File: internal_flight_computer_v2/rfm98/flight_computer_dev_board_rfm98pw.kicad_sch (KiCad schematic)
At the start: 95 parts, among them IC1 RP2040_QFN56, IC2 AZ1117CH-3.3TRG1, J1 Conn_ARM_JTAG_SWD_10, J10 BM04B-SRSS-TB(LF)(SN), J11 BM04B-SRSS-TB(LF)(SN), J12 BM04B-SRSS-TB(LF)(SN), J13 Breakout, J15 Battery, J2 FC to EPS Connector, J3 Life Makes Lemonade, J4 104031-0811, J5 BM04B-SRSS-TB(LF)(SN), J6 Conn_Coaxial, J7 Breakout, J8 USB_B_Micro, J9 BM04B-SRSS-TB(LF)(SN), SW1 KMR2, SW2 KMR2, U10 AP3602AKTR-G1, U3 MAX706RESA, U4 RFM98PW, U5 RFM9xBreakout, U6 W25Q128JV, U7 LSM6DSOTR, U8 LSM303AGRTR, U9 MCP25625-E/ML, Y1 12MHZ, Y3 16MHZ 12 pf

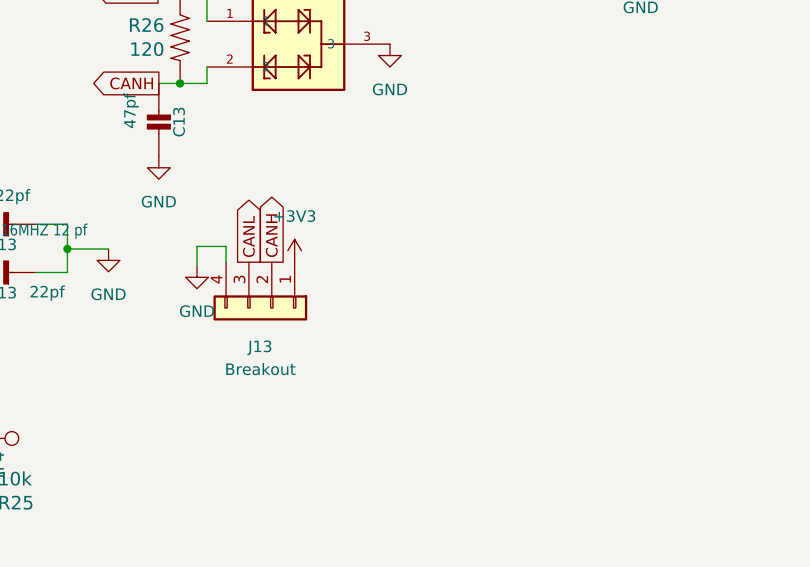
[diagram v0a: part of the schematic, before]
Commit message: Huge Restructure of Dev Boards
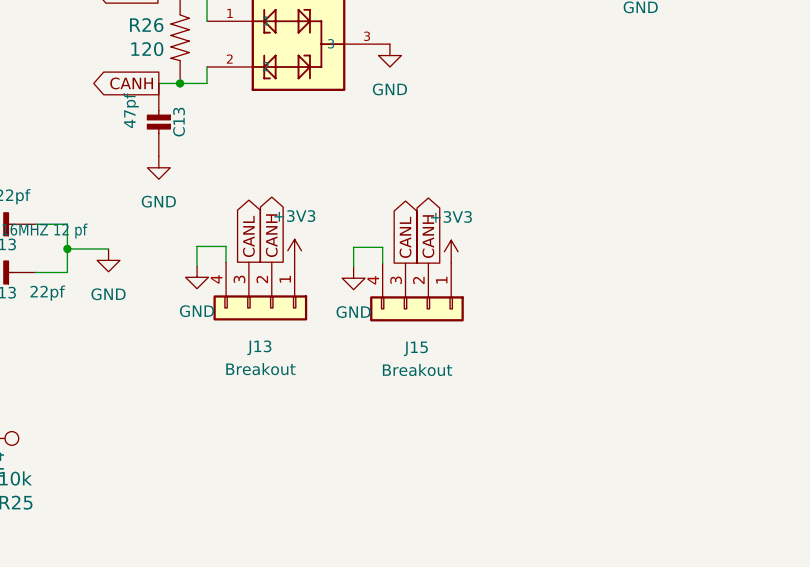
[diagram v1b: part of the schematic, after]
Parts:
- added J15: Breakout, Connector_JST:JST_SH_BM04B-SRSS-TB_1x04-1MP_P1.00mm_Vertical, symbol Connector_Generic:Conn_01x04
- J13: footprint Connector_JST:JST_SH_SM04B-SRSS-TB_1x04-1MP_P1.00mm_Horizontal -> Connector_JST:JST_SH_BM04B-SRSS-TB_1x04-1MP_P1.00mm_Vertical
- TP5: value RESET -> 5V
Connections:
- net +3V3: now also J15.1 (Pin_1)
- net CANH: now also J15.2 (Pin_2)
- net CANL: now also J15.3 (Pin_3)
- net GND: now also J15.4 (Pin_4)
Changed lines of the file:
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@@
     (stroke (width 0) (type default))
   )
+  (wire (pts (xy 406.8318 351.409) (xy 406.8318 353.1616))
+    (stroke (width 0) (type default))
+  )
   (wire (pts (xy 359.3592 348.9706) (xy 352.2218 348.9706))
     (stroke (width 0) (type default))
@@
     (stroke (width 0) (type default))
   )
+  (wire (pts (xy 403.606 351.409) (xy 406.8318 351.409))
+    (stroke (width 0) (type default))
+  )
   (wire (pts (xy 385.572 234.569) (xy 394.3604 234.569))
     (stroke (width 0) (type default))
@@
     (stroke (width 0) (type default))
   )
+  (wire (pts (xy 403.606 351.409) (xy 403.606 353.568))
+    (stroke (width 0) (type default))
+  )
   (wire (pts (xy 142.748 250.444) (xy 142.748 247.904))
     (stroke (width 0) (type default))
@@
     )
   )
+  (global_label "CANH" (shape output) (at 411.9118 353.1616 90) (fields_autoplaced)
+    (effects (font (size 1.27 1.27)) (justify left))
+    (property "Intersheetrefs" "${INTERSHEET_REFS}" (at 411.9118 345.2362 90)
+      (effects (font (size 1.27 1.27)) (justify left) hide)
+    )
+  )
   (global_label "CANL" (shape output) (at 391.9728 353.06 90) (fields_autoplaced)
     (effects (font (size 1.27 1.27)) (justify left))
@@
     )
   )
+  (global_label "CANL" (shape output) (at 409.3718 353.1616 90) (fields_autoplaced)
+    (effects (font (size 1.27 1.27)) (justify left))
+    (property "Intersheetrefs" "${INTERSHEET_REFS}" (at 409.3718 345.5386 90)
+      (effects (font (size 1.27 1.27)) (justify left) hide)
+    )
+  )
   (global_label "SDA0" (shape bidirectional) (at 153.924 131.826 0) (fields_autoplaced)
     (effects (font (size 1.27 1.27)) (justify left))
@@
     )
   )
+  (symbol (lib_id "power:GND") (at 403.606 353.568 0) (unit 1)
+    (in_bom yes) (on_board yes) (dnp no) (fields_autoplaced)
+    (property "Reference" "#PWR036" (at 403.606 359.918 0)
+      (effects (font (size 1.27 1.27)) hide)
+    )
+    (property "Value" "GND" (at 403.606 358.648 0)
+      (effects (font (size 1.27 1.27)))
+    )
+    (property "Footprint" "" (at 403.606 353.568 0)
+      (effects (font (size 1.27 1.27)) hide)
+    )
+    (property "Datasheet" "" (at 403.606 353.568 0)
+      (effects (font (size 1.27 1.27)) hide)
+    )
+    (pin "1")
+    (instances
+      (project "flight_computer_dev_board_rfm98pw"
+        (path "/c64c0d72-a9f6-4f3a-891e-1f647558f538"
+          (reference "#PWR036") (unit 1)
+        )
+      )
+    )
+  )
   (symbol (lib_id "Adafruit ItsyBitsy RP2040-eagle-import:+3V3") (at 153.543 34.925 0) (unit 1)
     (in_bom yes) (on_board yes) (dnp no) (fields_autoplaced)
@@
     )
   )
+  (symbol (lib_id "Connector_Generic:Conn_01x04") (at 411.9118 358.2416 270) (unit 1)
+    (in_bom yes) (on_board yes) (dnp no) (fields_autoplaced)
+    (property "Reference" "J15" (at 410.6418 362.5596 90)
+      (effects (font (size 1.27 1.27)))
+    )
+    (property "Value" "Breakout" (at 410.6418 365.0996 90)
+      (effects (font (size 1.27 1.27)))
+    )
+    (property "Footprint" "Connector_JST:JST_SH_BM04B-SRSS-TB_1x04-1MP_P1.00mm_Vertical" (at 411.9118 358.2416 0)
+      (effects (font (size 1.27 1.27)) hide)
+    )
+    (property "Datasheet" "~" (at 411.9118 358.2416 0)
+      (effects (font (size 1.27 1.27)) hide)
+    )
+    (pin "1")
+    (pin "2")
+    (pin "3")
+    (pin "4")
+    (instances
+      (project "flight_computer_dev_board_rfm98pw"
+        (path "/c64c0d72-a9f6-4f3a-891e-1f647558f538"
+          (reference "J15") (unit 1)
+        )
+      )
+    )
+  )
   (symbol (lib_id "Connector:TestPoint") (at 22.987 97.536 270) (unit 1)
     (in_bom yes) (on_board yes) (dnp no)
@@
       (effects (font (size 1.27 1.27)) (justify left))
     )
-    (property "Value" "RESET" (at 236.982 347.7768 0)
+    (property "Value" "5V" (at 236.982 347.7768 0)
       (effects (font (size 1.27 1.27)) (justify left) hide)
     )
@@
     )
   )
+  (symbol (lib_id "power:+3V3") (at 414.4518 353.1616 0) (unit 1)
+    (in_bom yes) (on_board yes) (dnp no) (fields_autoplaced)
+    (property "Reference" "#PWR037" (at 414.4518 356.9716 0)
+      (effects (font (size 1.27 1.27)) hide)
+    )
+    (property "Value" "+3V3" (at 414.4518 348.0816 0)
+      (effects (font (size 1.27 1.27)))
+    )
+    (property "Footprint" "" (at 414.4518 353.1616 0)
+      (effects (font (size 1.27 1.27)) hide)
+    )
+    (property "Datasheet" "" (at 414.4518 353.1616 0)
+      (effects (font (size 1.27 1.27)) hide)
+    )
+    (pin "1")
+    (instances
+      (project "flight_computer_dev_board_rfm98pw"
+        (path "/c64c0d72-a9f6-4f3a-891e-1f647558f538"
+          (reference "#PWR037") (unit 1)
+        )
+      )
+    )
+  )
   (symbol (lib_id "BM04B-SRSS-TB_LF__SN_:BM04B-SRSS-TB(LF)(SN)") (at 221.615 74.676 0) (unit 1)
     (in_bom yes) (on_board yes) (dnp no) (fields_autoplaced)
@@
       (effects (font (size 1.27 1.27)))
     )
-    (property "Footprint" "Connector_JST:JST_SH_SM04B-SRSS-TB_1x04-1MP_P1.00mm_Horizontal" (at 394.5128 358.14 0)
+    (property "Footprint" "Connector_JST:JST_SH_BM04B-SRSS-TB_1x04-1MP_P1.00mm_Vertical" (at 394.5128 358.14 0)
       (effects (font (size 1.27 1.27)) hide)
     )

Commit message: Big Update of In Dev Boards
Mid Term update for all the boards being developed for use by the Irvington Team on Pleiades - Orpheus
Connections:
- net USBBOOT is gone; now on net D3: D4.1 (K), IC1.16 (GPIO13), SW1.A (P), SW1.A' (P1), TP1.1
- net 3v3 Spec: no longer LED1.1 (VDD)
- net D6: now also IC1.27 (GPIO16); no longer IC1.29 (GPIO18)
- net D8: now also IC1.29 (GPIO18); no longer IC1.30 (GPIO19)
- net D9: now also IC1.30 (GPIO19); no longer IC1.39 (GPIO27/AD1)
- net BURN_RELAY_A / VS renamed BURN_RELAY_A / D5
- net BURN_RELAY_A / D5: now also JP9.3 (B); no longer J2.2 (Pin_2)
- net D4 renamed VBUS_RESET / D4
- net VBUS_RESET / D4: now also IC1.17 (GPIO14); no longer IC1.27 (GPIO16)
- net D5 renamed D7
- net D7: now also J2.9 (Pin_9); no longer JP9.3 (B)
- net ENABLE_BURN / D7 renamed ENABLE_BURN / PC
- net ENABLE_BURN / PC: now also J2.3 (Pin_3); no longer J2.9 (Pin_9)
- net ENAB_RF / D3 renamed D3
- net D3: no longer IC1.15 (GPIO12)
- net I2C_RESET / D2 renamed ENAB_RF / D2
- net ENAB_RF / D2: now also IC1.15 (GPIO12); no longer IC1.9 (GPIO7)
- removed net VBUS_RESET / PC: IC1.17 (GPIO14), J2.3 (Pin_3)
- new net I2C_RESET / VS: IC1.9 (GPIO7), J2.2 (Pin_2)
- new net Neo_pwr: IC1.39 (GPIO27/AD1), LED1.1 (VDD)
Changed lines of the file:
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@@
     )
   )
-  (global_label "BURN_RELAY_A {slash} VS" (shape output) (at 160.274 162.306 0) (fields_autoplaced)
-    (effects (font (size 1.27 1.27)) (justify left))
-    (property "Intersheetrefs" "${INTERSHEET_REFS}" (at 182.5927 162.306 0)
+  (global_label "BURN_RELAY_A {slash} D5" (shape output) (at 160.274 162.306 0) (fields_autoplaced)
+    (effects (font (size 1.27 1.27)) (justify left))
+    (property "Intersheetrefs" "${INTERSHEET_REFS}" (at 182.7741 162.306 0)
       (effects (font (size 1.27 1.27)) (justify left) hide)
     )
@@
     )
   )
-  (global_label "ENAB_RF {slash} D3" (shape input) (at 347.472 286.004 180) (fields_autoplaced)
-    (effects (font (size 1.27 1.27)) (justify right))
-    (property "Intersheetrefs" "${INTERSHEET_REFS}" (at 330.6567 286.004 0)
-      (effects (font (size 1.27 1.27)) (justify right) hide)
-    )
-  )
-  (global_label "I2C_RESET {slash} D2" (shape output) (at 153.924 139.446 0) (fields_autoplaced)
-    (effects (font (size 1.27 1.27)) (justify left))
-    (property "Intersheetrefs" "${INTERSHEET_REFS}" (at 172.372 139.446 0)
+  (global_label "D3" (shape input) (at 347.472 286.004 180) (fields_autoplaced)
+    (effects (font (size 1.27 1.27)) (justify right))
+    (property "Intersheetrefs" "${INTERSHEET_REFS}" (at 342.0867 286.004 0)
+      (effects (font (size 1.27 1.27)) (justify right) hide)
+    )
+  )
+  (global_label "I2C_RESET {slash} VS" (shape output) (at 153.924 139.446 0) (fields_autoplaced)
+    (effects (font (size 1.27 1.27)) (justify left))
+    (property "Intersheetrefs" "${INTERSHEET_REFS}" (at 172.1906 139.446 0)
       (effects (font (size 1.27 1.27)) (justify left) hide)
     )
@@
     )
   )
-  (global_label "D5" (shape input) (at 146.304 169.926 0) (fields_autoplaced)
+  (global_label "D7" (shape input) (at 146.304 169.926 0) (fields_autoplaced)
     (effects (font (size 1.27 1.27)) (justify left))
     (property "Intersheetrefs" "${INTERSHEET_REFS}" (at 151.6893 169.926 0)
@@
     (property "Intersheetrefs" "${INTERSHEET_REFS}" (at 212.725 62.4688 90)
       (effects (font (size 1.27 1.27)) (justify right) hide)
+    )
+  )
+  (global_label "D3" (shape input) (at 159.004 157.226 0) (fields_autoplaced)
+    (effects (font (size 1.27 1.27)) (justify left))
+    (property "Intersheetrefs" "${INTERSHEET_REFS}" (at 164.3893 157.226 0)
+      (effects (font (size 1.27 1.27)) (justify left) hide)
     )
   )
@@
     )
   )
-  (global_label "VBUS_RESET {slash} PC" (shape output) (at 160.274 159.766 0) (fields_autoplaced)
-    (effects (font (size 1.27 1.27)) (justify left))
-    (property "Intersheetrefs" "${INTERSHEET_REFS}" (at 180.5968 159.766 0)
+  (global_label "VBUS_RESET {slash} D4" (shape output) (at 160.274 159.766 0) (fields_autoplaced)
+    (effects (font (size 1.27 1.27)) (justify left))
+    (property "Intersheetrefs" "${INTERSHEET_REFS}" (at 180.5363 159.766 0)
       (effects (font (size 1.27 1.27)) (justify left) hide)
     )
@@
     )
   )
-  (global_label "D8" (shape input) (at 146.304 175.006 0) (fields_autoplaced)
+  (global_label "D9" (shape input) (at 146.304 175.006 0) (fields_autoplaced)
     (effects (font (size 1.27 1.27)) (justify left))
     (property "Intersheetrefs" "${INTERSHEET_REFS}" (at 151.6893 175.006 0)
@@
     )
   )
-  (global_label "I2C_RESET {slash} D2" (shape input) (at 347.472 283.464 180) (fields_autoplaced)
-    (effects (font (size 1.27 1.27)) (justify right))
-    (property "Intersheetrefs" "${INTERSHEET_REFS}" (at 329.024 283.464 0)
+  (global_label "ENAB_RF {slash} D2" (shape input) (at 347.472 283.464 180) (fields_autoplaced)
+    (effects (font (size 1.27 1.27)) (justify right))
+    (property "Intersheetrefs" "${INTERSHEET_REFS}" (at 330.6567 283.464 0)
       (effects (font (size 1.27 1.27)) (justify right) hide)
     )
@@
     )
   )
-  (global_label "VBUS_RESET {slash} PC" (shape bidirectional) (at 347.472 280.924 180) (fields_autoplaced)
-    (effects (font (size 1.27 1.27)) (justify right))
-    (property "Intersheetrefs" "${INTERSHEET_REFS}" (at 326.0379 280.924 0)
+  (global_label "ENABLE_BURN {slash} PC" (shape bidirectional) (at 347.472 280.924 180) (fields_autoplaced)
+    (effects (font (size 1.27 1.27)) (justify right))
+    (property "Intersheetrefs" "${INTERSHEET_REFS}" (at 324.4654 280.924 0)
       (effects (font (size 1.27 1.27)) (justify right) hide)
     )
@@
     )
   )
-  (global_label "ENAB_RF {slash} D3" (shape bidirectional) (at 160.02 154.686 0) (fields_autoplaced)
+  (global_label "ENAB_RF {slash} D2" (shape bidirectional) (at 160.02 154.686 0) (fields_autoplaced)
     (effects (font (size 1.27 1.27)) (justify left))
     (property "Intersheetrefs" "${INTERSHEET_REFS}" (at 177.9466 154.686 0)
@@
     )
   )
-  (global_label "D5" (shape input) (at 285.4452 283.464 0) (fields_autoplaced)
-    (effects (font (size 1.27 1.27)) (justify left))
-    (property "Intersheetrefs" "${INTERSHEET_REFS}" (at 290.8305 283.464 0)
+  (global_label "BURN_RELAY_A {slash} D5" (shape input) (at 285.4452 283.464 0) (fields_autoplaced)
+    (effects (font (size 1.27 1.27)) (justify left))
+    (property "Intersheetrefs" "${INTERSHEET_REFS}" (at 307.9453 283.464 0)
       (effects (font (size 1.27 1.27)) (justify left) hide)
     )
@@
     )
   )
-  (global_label "D4" (shape input) (at 281.9908 271.7292 0) (fields_autoplaced)
-    (effects (font (size 1.27 1.27)) (justify left))
-    (property "Intersheetrefs" "${INTERSHEET_REFS}" (at 287.3761 271.7292 0)
+  (global_label "VBUS_RESET {slash} D4" (shape input) (at 281.9908 271.7292 0) (fields_autoplaced)
+    (effects (font (size 1.27 1.27)) (justify left))
+    (property "Intersheetrefs" "${INTERSHEET_REFS}" (at 302.2531 271.7292 0)
       (effects (font (size 1.27 1.27)) (justify left) hide)
     )
@@
     )
   )
-  (global_label "BURN_RELAY_A {slash} VS" (shape input) (at 347.472 278.384 180) (fields_autoplaced)
-    (effects (font (size 1.27 1.27)) (justify right))
-    (property "Intersheetrefs" "${INTERSHEET_REFS}" (at 325.1533 278.384 0)
+  (global_label "I2C_RESET {slash} VS" (shape input) (at 347.472 278.384 180) (fields_autoplaced)
+    (effects (font (size 1.27 1.27)) (justify right))
+    (property "Intersheetrefs" "${INTERSHEET_REFS}" (at 329.2054 278.384 0)
       (effects (font (size 1.27 1.27)) (justify right) hide)
     )
@@
     )
   )
-  (global_label "D9" (shape input) (at 70.104 172.466 180) (fields_autoplaced)
-    (effects (font (size 1.27 1.27)) (justify right))
-    (property "Intersheetrefs" "${INTERSHEET_REFS}" (at 64.7187 172.466 0)
+  (global_label "Neo_pwr" (shape input) (at 70.104 172.466 180) (fields_autoplaced)
+    (effects (font (size 1.27 1.27)) (justify right))
+    (property "Intersheetrefs" "${INTERSHEET_REFS}" (at 59.3968 172.466 0)
       (effects (font (size 1.27 1.27)) (justify right) hide)
     )
@@
     )
   )
-  (global_label "ENABLE_BURN {slash} D7" (shape input) (at 347.472 296.164 180) (fields_autoplaced)
-    (effects (font (size 1.27 1.27)) (justify right))
-    (property "Intersheetrefs" "${INTERSHEET_REFS}" (at 325.6372 296.164 0)
-      (effects (font (size 1.27 1.27)) (justify right) hide)
-    )
-  )
-  (global_label "ENABLE_BURN {slash} D7" (shape output) (at 153.924 136.906 0) (fields_autoplaced)
-    (effects (font (size 1.27 1.27)) (justify left))
-    (property "Intersheetrefs" "${INTERSHEET_REFS}" (at 175.7588 136.906 0)
+  (global_label "D7" (shape input) (at 347.472 296.164 180) (fields_autoplaced)
+    (effects (font (size 1.27 1.27)) (justify right))
+    (property "Intersheetrefs" "${INTERSHEET_REFS}" (at 342.0867 296.164 0)
+      (effects (font (size 1.27 1.27)) (justify right) hide)
+    )
+  )
+  (global_label "ENABLE_BURN {slash} PC" (shape output) (at 153.924 136.906 0) (fields_autoplaced)
+    (effects (font (size 1.27 1.27)) (justify left))
+    (property "Intersheetrefs" "${INTERSHEET_REFS}" (at 175.8193 136.906 0)
       (effects (font (size 1.27 1.27)) (justify left) hide)
     )
@@
     )
   )
-  (global_label "D6" (shape input) (at 146.304 172.466 0) (fields_autoplaced)
+  (global_label "D8" (shape input) (at 146.304 172.466 0) (fields_autoplaced)
     (effects (font (size 1.27 1.27)) (justify left))
     (property "Intersheetrefs" "${INTERSHEET_REFS}" (at 151.6893 172.466 0)
@@
     )
   )
+  (global_label "Neo_pwr" (shape input) (at 275.082 35.433 90) (fields_autoplaced)
+    (effects (font (size 1.27 1.27)) (justify left))
+    (property "Intersheetrefs" "${INTERSHEET_REFS}" (at 275.082 24.7258 90)
+      (effects (font (size 1.27 1.27)) (justify left) hide)
+    )
+  )
   (global_label "SDA1" (shape bidirectional) (at 165.735 105.029 270) (fields_autoplaced)
     (effects (font (size 1.27 1.27)) (justify right))
@@
     )
   )
-  (global_label "D4" (shape input) (at 146.304 167.386 0) (fields_autoplaced)
+  (global_label "D6" (shape input) (at 146.304 167.386 0) (fields_autoplaced)
     (effects (font (size 1.27 1.27)) (justify left))
     (property "Intersheetrefs" "${INTERSHEET_REFS}" (at 151.6893 167.386 0)
@@
       (effects (font (size 1.27 1.27)) (justify left) hide)
     )
-  )
-  (global_label "3v3 Spec" (shape input) (at 275.082 35.433 90) (fields_autoplaced)
-    (effects (font (size 1.27 1.27)) (justify left))
-    (property "Intersheetrefs" "${INTERSHEET_REFS}" (at 275.082 23.6373 90)
-      (effects (font (size 1.27 1.27)) (justify left) hide)
-    )
